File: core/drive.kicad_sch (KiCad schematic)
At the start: 31 parts, among them Q3 BSS84, Q4 MMBT3904, Q5 MMBT3904, Q6 MMBT3906, Q7 MMBT3906, Q8 MMBT3904, U3 TL072, U4 TL072

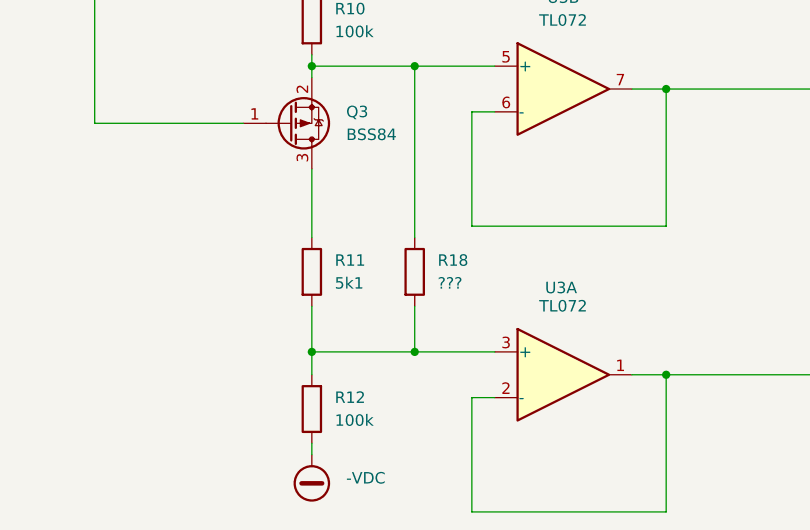
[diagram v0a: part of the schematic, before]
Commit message: Tweak resistor values
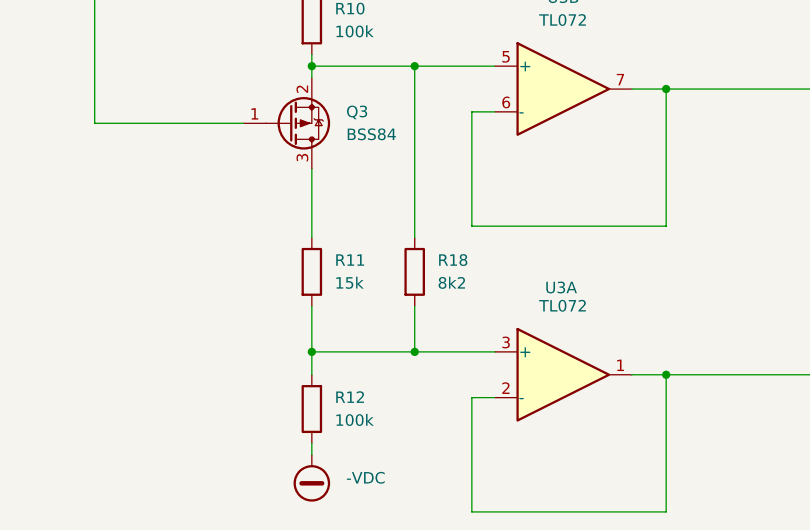
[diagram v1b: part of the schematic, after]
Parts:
- R11: value 5k1 -> 15k
- R18: value ??? -> 8k2
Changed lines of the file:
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@@
 			)
 		)
-		(property "Value" "5k1"
+		(property "Value" "15k"
 			(at 76.2 167.6399 0)
 			(effects
@@
 			)
 		)
-		(property "Value" "???"
+		(property "Value" "8k2"
 			(at 87.63 167.6399 0)
 			(effects

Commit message: Update partnames
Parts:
- D1, D2, D3, D4, D5, D6: value D -> 1N4148
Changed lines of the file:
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@@
 			)
 		)
-		(property "Value" "D"
+		(property "Value" "1N4148"
 			(at 119.38 95.25 0)
 			(effects
@@
 			)
 		)
-		(property "Value" "D"
+		(property "Value" "1N4148"
 			(at 167.64 80.0099 90)
 			(effects
@@
 			)
 		)
-		(property "Value" "D"
+		(property "Value" "1N4148"
 			(at 167.64 92.7099 90)
 			(effects
@@
 			)
 		)
-		(property "Value" "D"
+		(property "Value" "1N4148"
 			(at 110.49 62.23 0)
 			(effects
@@
 			)
 		)
-		(property "Value" "D"
+		(property "Value" "1N4148"
 			(at 109.22 95.25 0)
 			(effects
@@
 			)
 		)
-		(property "Value" "D"
+		(property "Value" "1N4148"
 			(at 120.65 62.23 0)
 			(effects

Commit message: Fixes for v1.1
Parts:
- removed D5, D6: 1N4148, Diode_SMD:D_SOD-323_HandSoldering, symbol Device:D
- removed Q3: BSS84, Package_TO_SOT_SMD:SOT-23, symbol Transistor_FET:BSS84
- removed R11: 15k, Resistor_SMD:R_0603_1608Metric, symbol Device:R
- added Q8: MMBT3906, Package_TO_SOT_SMD:SOT-23, symbol Transistor_BJT:MMBT3906
- added Q9: MMBT3904, Package_TO_SOT_SMD:SOT-23, symbol Transistor_BJT:MMBT3904
- R12: renamed from R18; value 8k2 -> 4k3
- R18: renamed from R22; value 3k3 -> 2k
- R19: renamed from R23; value 15k -> 18k
- renumbered Q4 to Q3, Q5 to Q4, Q6 to Q5, Q7 to Q6, Q8 to Q7, R13 to R10, R10 to R11, R12 to R13, R24 to R20
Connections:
- net +VDC: now also Q9.3 (C)
- net -VDC: now also Q8.3 (C)
- net at R18.2, R19.1: now also Q6.2 (E), Q7.2 (E), R14.2, Q8.2 (E), Q9.2 (E)
- net at U3.6 (-), U3.7: now also Q8.1 (B)
- net at U3.1, U3.2 (-): now also Q9.1 (B)
- new net: R18.1, U4.1
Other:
- moved on the sheet: C5, C6, C7, C8, D1, D2, D3, D4, Q3, Q4, Q5, Q6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
